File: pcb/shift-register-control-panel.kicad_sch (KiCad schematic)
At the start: 30 parts, among them J1 Conn_01x08, J2 USB_A, SW1 INPUT, SW2 SHIFT, SW3 CLEAR, SW4 DISPLAY, U1 74HC595, U2 LM7805_TO220

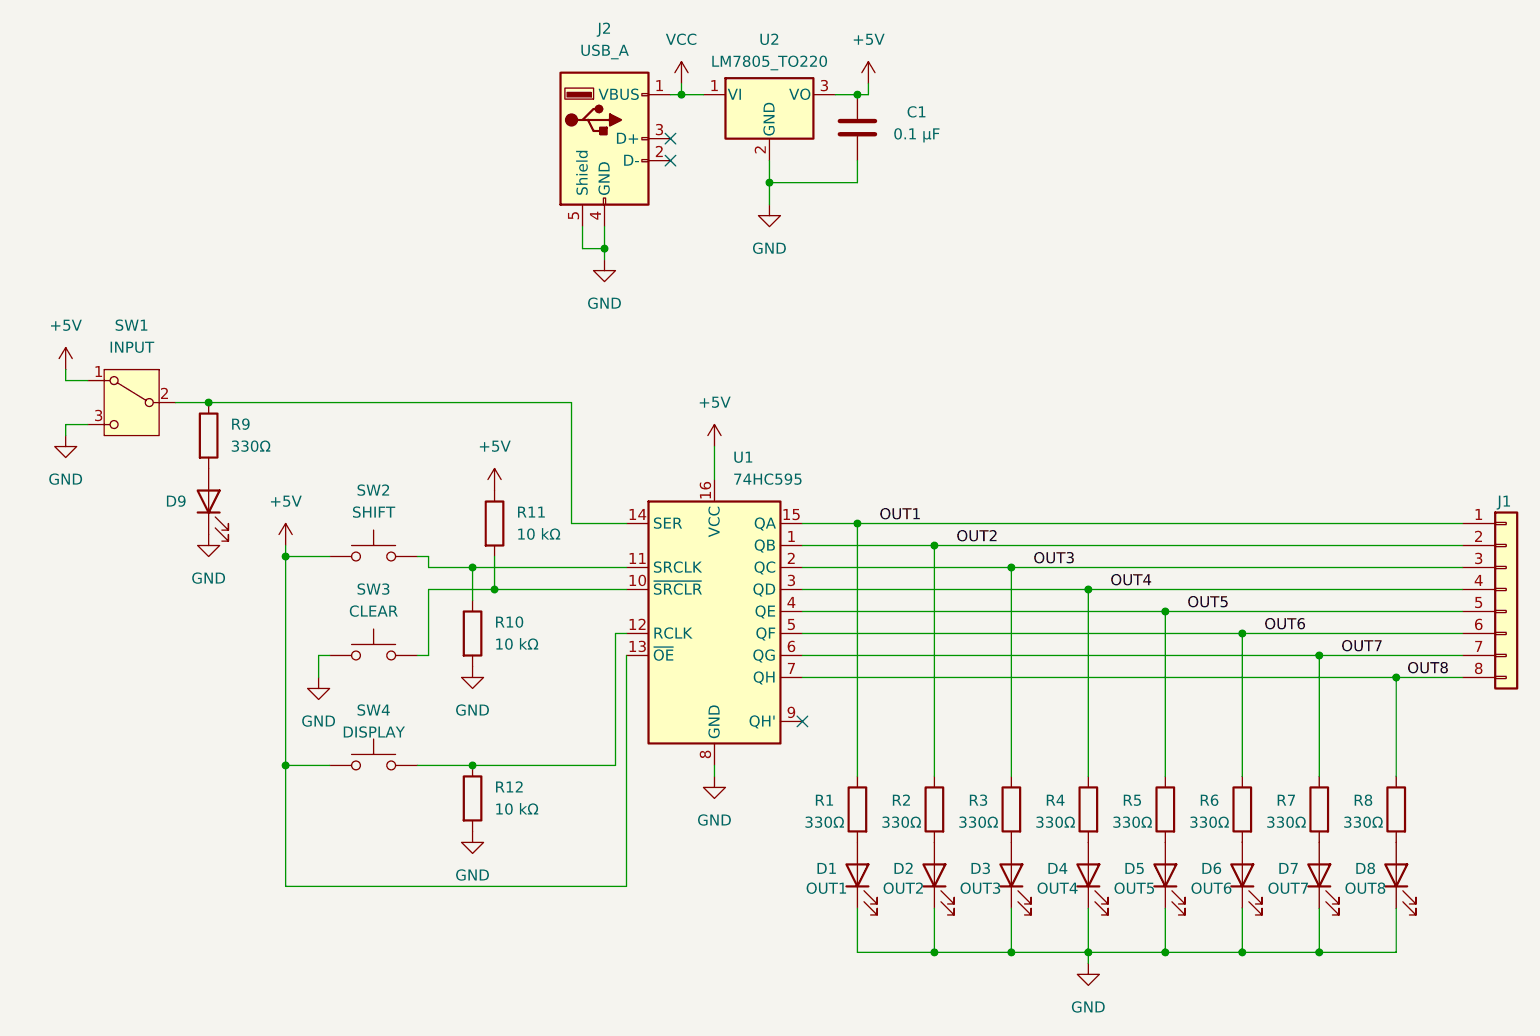
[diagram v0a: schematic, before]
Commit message: added debounce to shift input
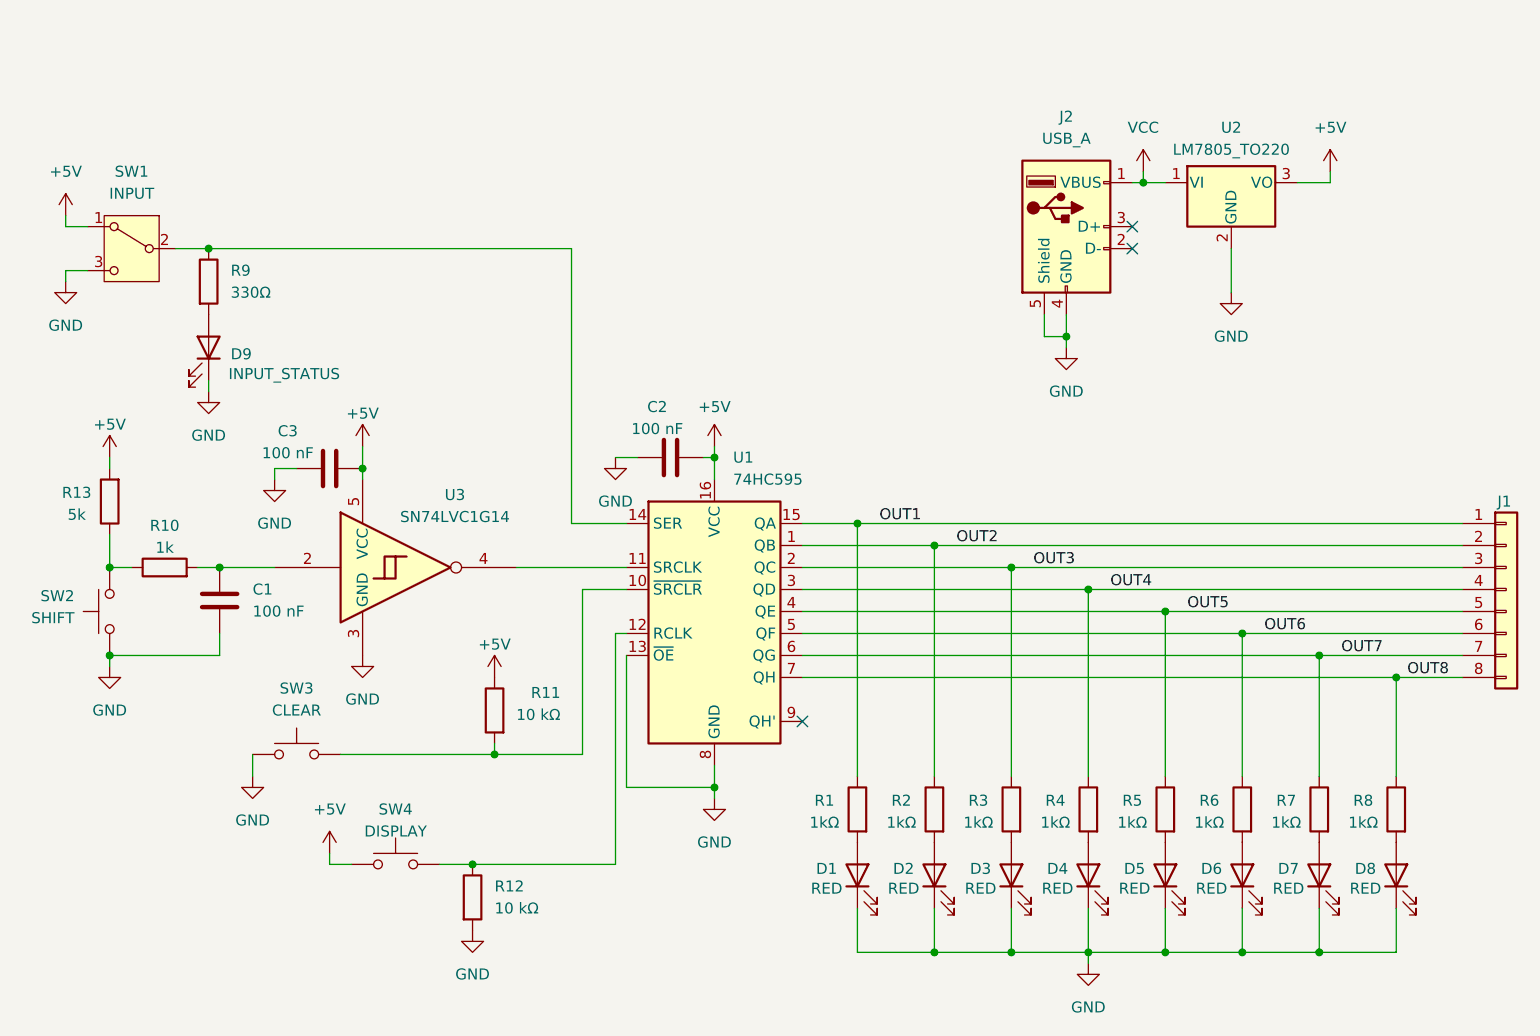
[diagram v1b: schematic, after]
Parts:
- added C2, C3: 100 nF, Capacitor_THT:C_Disc_D5.0mm_W2.5mm_P5.00mm, symbol Device:C
- added R13: 5k, Resistor_THT:R_Axial_DIN0204_L3.6mm_D1.6mm_P5.08mm_Horizontal, symbol Device:R
- added U3: SN74LVC1G14, Package_TO_SOT_SMD:SOT-23-5, symbol 74xGxx:SN74LVC1G14DBV
- C1: value 0.1 µF -> 100 nF; footprint Capacitor_THT:C_Radial_D5.0mm_H7.0mm_P2.00mm -> Capacitor_THT:C_Disc_D5.0mm_W2.5mm_P5.00mm
- D1: value OUT1 -> RED
- D2: value OUT2 -> RED
- D3: value OUT3 -> RED
- D4: value OUT4 -> RED
- D5: value OUT5 -> RED
- D6: value OUT6 -> RED
- D7: value OUT7 -> RED
- D8: value OUT8 -> RED
- D9: value LED -> INPUT_STATUS
- R1, R2, R3, R4, R5, R6, R7, R8: value 330Ω -> 1kΩ
- R10: value 10 kΩ -> 1k
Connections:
- net +5V: now also C2.2, C3.2, R13.2, U3.5 (VCC); no longer C1.2, SW2.1, U1.13 (~{OE})
- net GND: now also C1.2, SW2.1, U1.13 (~{OE}), C2.1, C3.1, U3.3 (GND); no longer C1.1, R10.2
- net at R10.1, SW2.2: now also R13.1; no longer U1.11 (SRCLK)
- new net: C1.1, R10.2, U3.2
- new net: U1.11 (SRCLK), U3.4
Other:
- moved on the sheet: D9, J2, R11, R12, R9, SW1, SW3, SW4, U2
